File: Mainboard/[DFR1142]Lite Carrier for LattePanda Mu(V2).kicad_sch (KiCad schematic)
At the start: 6 parts

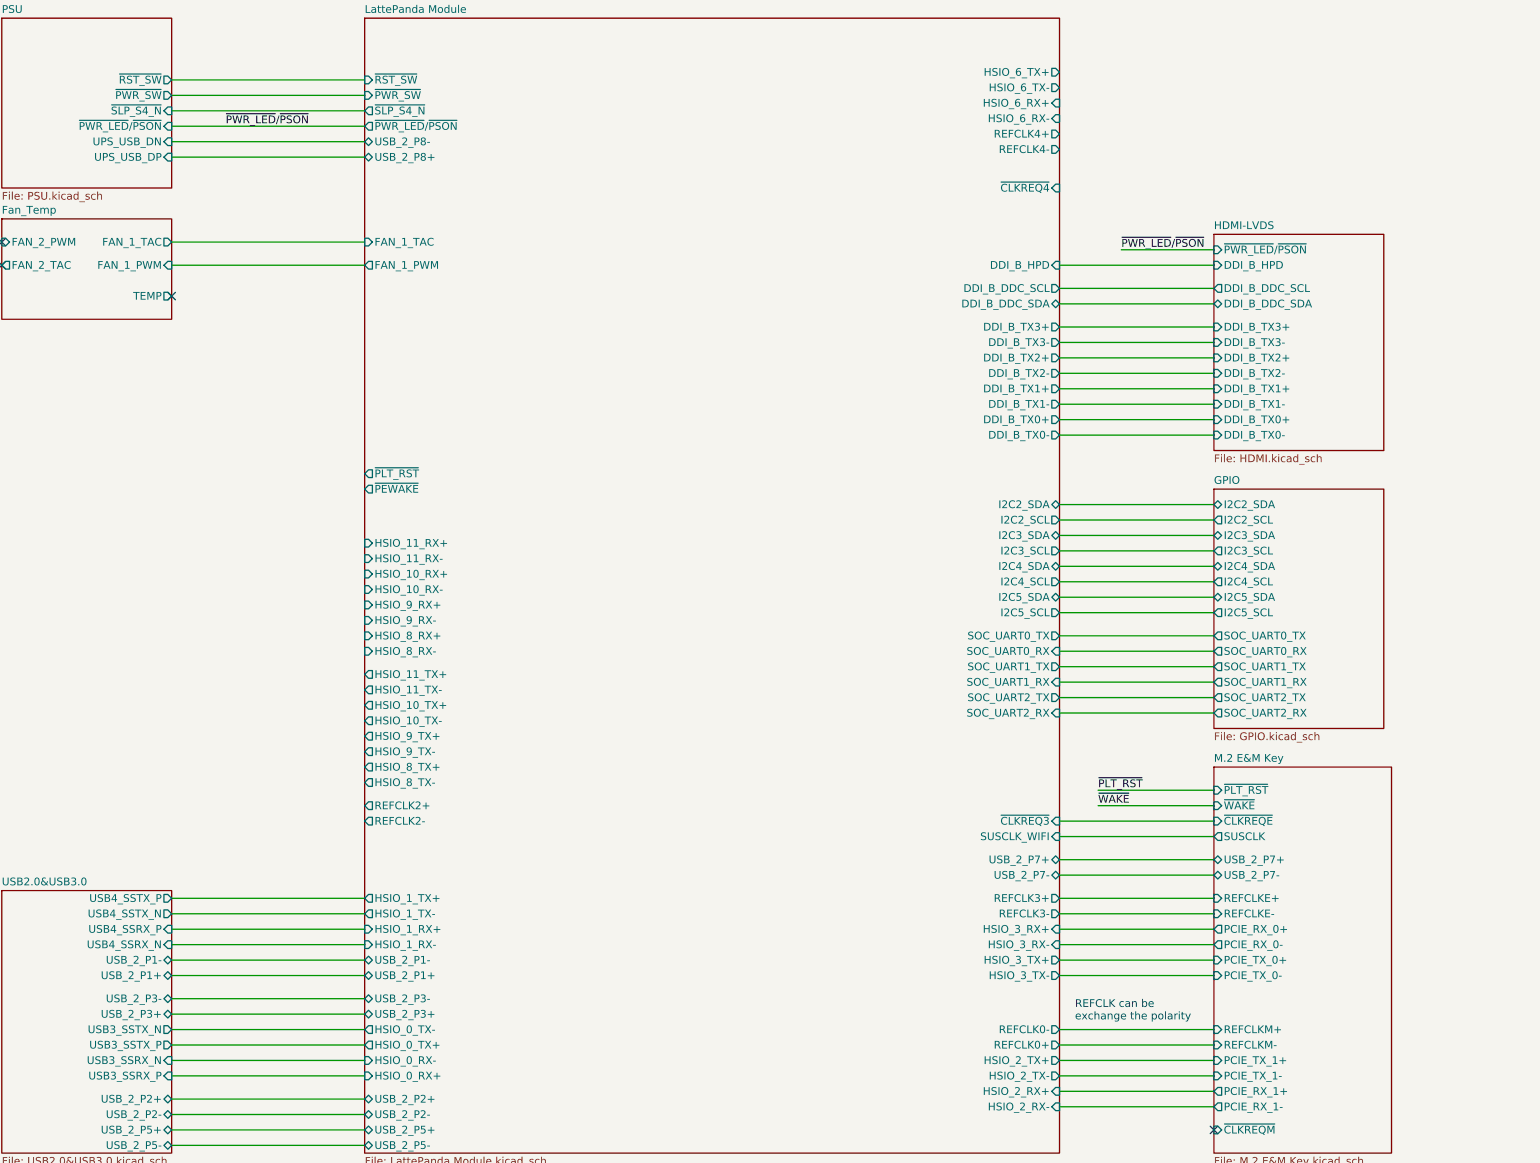
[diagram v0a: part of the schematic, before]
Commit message: Added HDMI > LDVS screens
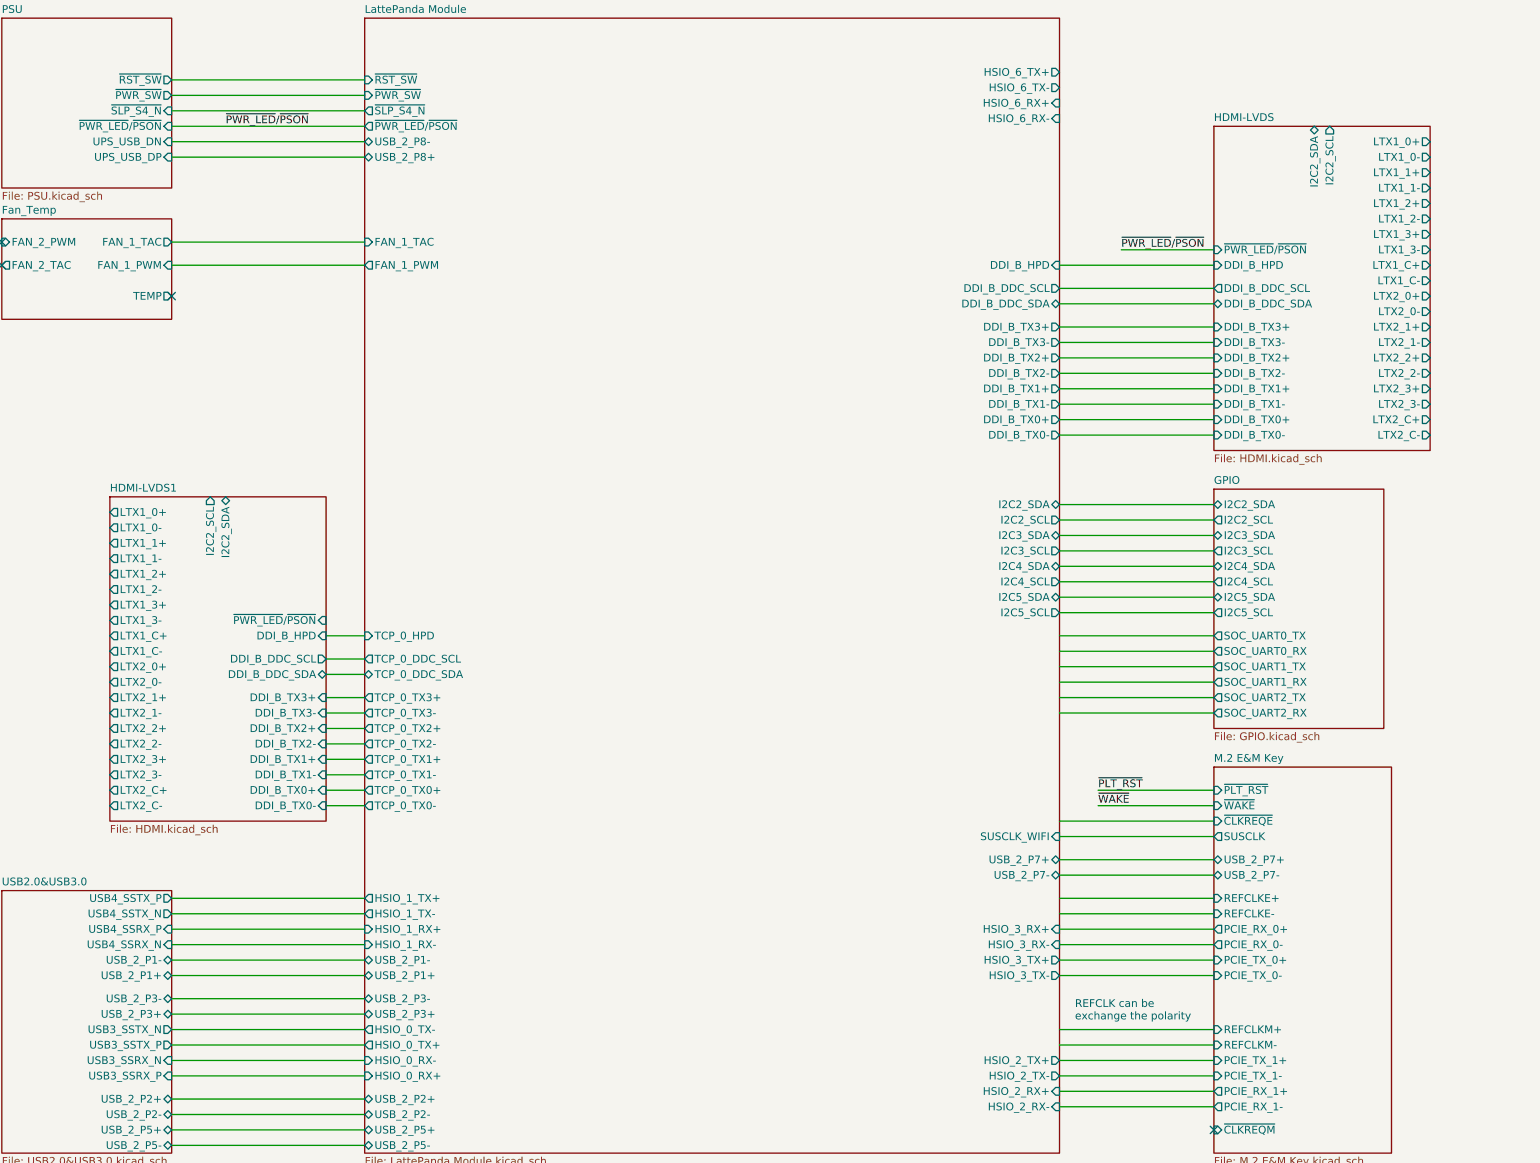
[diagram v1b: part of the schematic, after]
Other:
- added sheet HDMI-LVDS1 (HDMI.kicad_sch)
- sheet HDMI-LVDS ports: added I2C2_SCL, I2C2_SDA, LTX1_0+, LTX1_0-, LTX1_1+, LTX1_1-, LTX1_2+, LTX1_2-, LTX1_3+, LTX1_3-, LTX1_C+, LTX1_C-, LTX2_0+, LTX2_0-, LTX2_1+, LTX2_1-, LTX2_2+, LTX2_2-, LTX2_3+, LTX2_3-, LTX2_C+, LTX2_C-; removed none
- sheet LattePanda Module ports: added TCP_0_DDC_SCL, TCP_0_DDC_SDA, TCP_0_HPD, TCP_0_TX0+, TCP_0_TX0-, TCP_0_TX1+, TCP_0_TX1-, TCP_0_TX2+, TCP_0_TX2-, TCP_0_TX3+, TCP_0_TX3-; removed HSIO_10_RX+, HSIO_10_RX-, HSIO_10_TX+, HSIO_10_TX-, HSIO_11_RX+, HSIO_11_RX-, HSIO_11_TX+, HSIO_11_TX-, HSIO_8_RX+, HSIO_8_RX-, HSIO_8_TX+, HSIO_8_TX-, HSIO_9_RX+, HSIO_9_RX-, HSIO_9_TX+, HSIO_9_TX-, REFCLK0+, REFCLK0-, REFCLK2+, REFCLK2-, REFCLK3+, REFCLK3-, REFCLK4+, REFCLK4-, SOC_UART0_RX, SOC_UART0_TX, SOC_UART1_RX, SOC_UART1_TX, SOC_UART2_RX, SOC_UART2_TX, ~{CLKREQ3}, ~{CLKREQ4}, ~{PEWAKE}, ~{PLT_RST}

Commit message: More work on the Screens
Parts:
- added J20: 200485-0710, 200485-0710:2004850710, symbol 200485-0710:200485-0710
- added J3: 2004850740, 200485-0740:CON_2004850740, symbol 200485-0740:2004850740
- added R31: 10k, symbol Device:R
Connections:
- net GND: now also J20.1, J20.10, J20.G1 (GND_1), J20.G2 (GND_2), J20.MP1, J20.MP2, J20.MP3, J20.MP4, J3.10, J3.13, J3.16, J3.19, J3.22, J3.25, J3.30, J3.7
- net HDMI-LVDS/I2C2_SCL: now also J20.3
- net HDMI-LVDS/I2C2_SDA: now also J20.5
- net HDMI-LVDS/LTX1_0+: now also J3.9
- net HDMI-LVDS/LTX1_0-: now also J3.8
- net HDMI-LVDS/LTX1_1+: now also J3.12
- net HDMI-LVDS/LTX1_1-: now also J3.11
- net HDMI-LVDS/LTX1_2+: now also J3.15
- net HDMI-LVDS/LTX1_2-: now also J3.14
- net HDMI-LVDS/LTX1_3+: now also J3.21
- net HDMI-LVDS/LTX1_3-: now also J3.20
- net HDMI-LVDS/LTX1_C+: now also J3.18
- net HDMI-LVDS/LTX1_C-: now also J3.17
- new net: J20.7, R31.1
- new net +3V3: J20.2, J3.2, J3.3, R31.2
- no-connect marks 4 -> 25

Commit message: Mainboard Progress, Updated CTRL-L for new Joystick Module
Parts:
- added C40: 1uF, A_HDJ_Library:C_0603_1608Metric, symbol Device:C
- added C41: 4.7uF, A_HDJ_Library:C_0603_1608Metric, symbol Device:C
- added C42: 220nF, A_HDJ_Library:C_0603_1608Metric, symbol Device:C
- added D38: D, Diode_SMD:D_01005_0402Metric, symbol Device:D
- added L3: A915_Y-100M, symbol Device:L
- added R133: 0.57Ohm, Inductor_SMD:L_01005_0402Metric, symbol Device:R
- added U21: TPS61165DBV, Package_SON:WSON-6-1EP_2x2mm_P0.65mm_EP1x1.6mm, symbol Driver_LED:TPS61165DBV
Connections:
- net +3V3: now also J3.33, J3.34, J3.5, J3.6
- net GND: now also J3.G1, J3.G2, J3.P1, J3.P2, J3.P3, J3.P4, C40.1, C41.1, C42.1, U21.4 (GND)
- net LED-: now reaches J3.31
- net LED-: now also J3.32, R133.2
- net LED+: now reaches J3.39
- net LED+: now also J3.40, C40.2, D38.1 (K)
- new net: D38.2 (A), L3.2, U21.3 (SW)
- new net: C42.2, U21.5 (COMP)
- new net: R133.1, U21.6 (FB)
- new net +5V: C41.2, L3.1, U21.1 (VIN)
- new net SL_BRI: U21.2 (CTRL)
- no-connect marks 25 -> 29
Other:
- moved on the sheet: J3
